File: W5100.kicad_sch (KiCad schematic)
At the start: 8 parts, among them U2 W5100

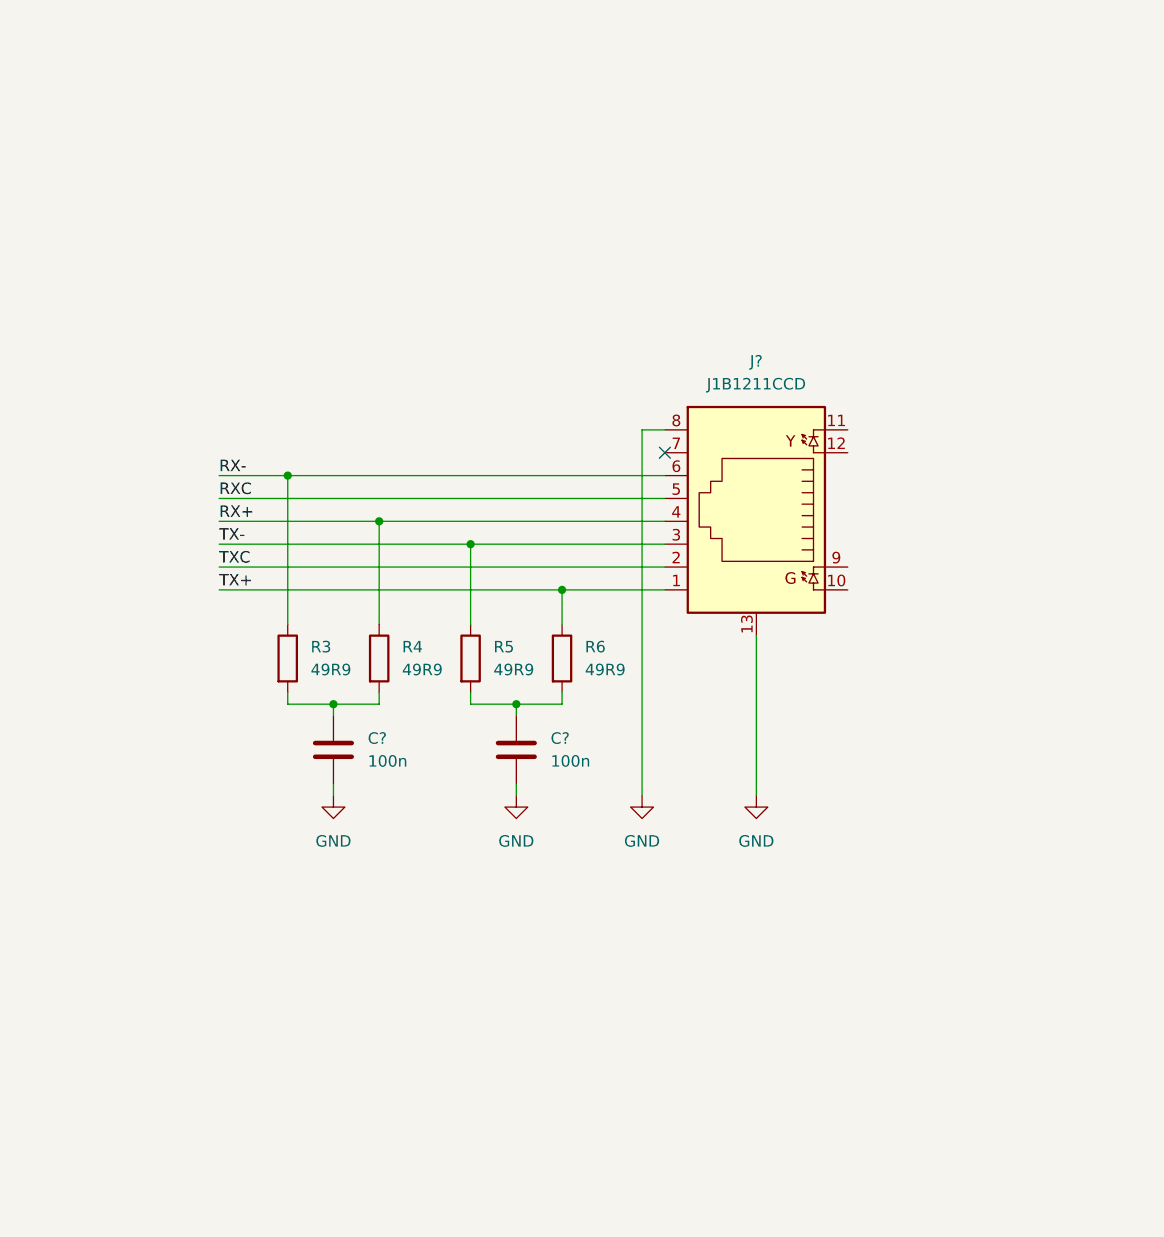
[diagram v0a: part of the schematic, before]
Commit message: Added RJ45
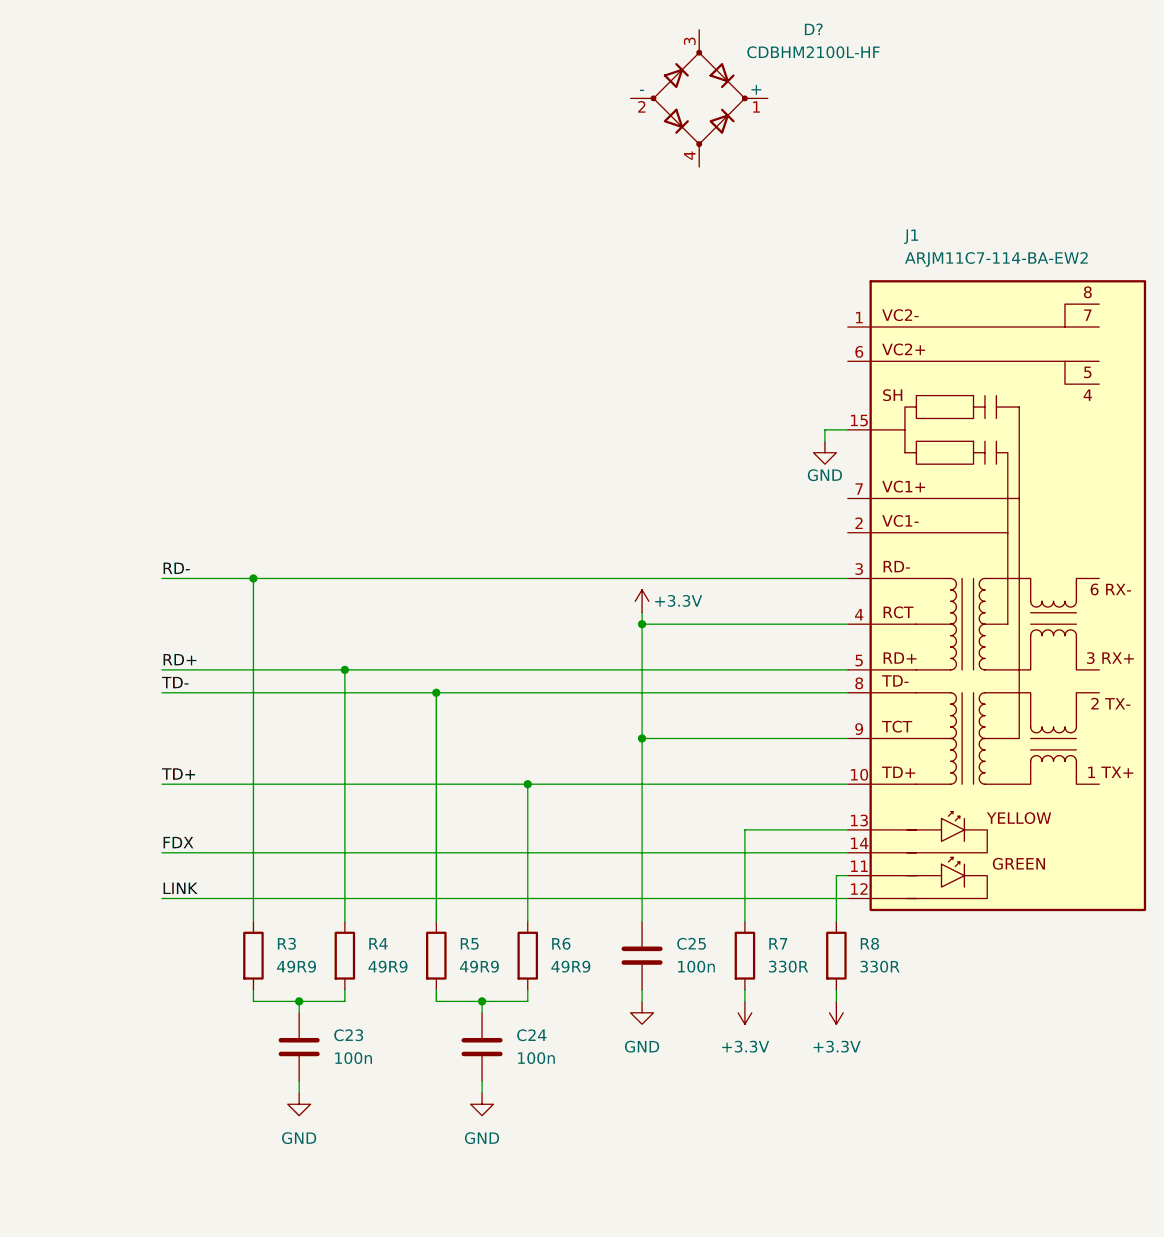
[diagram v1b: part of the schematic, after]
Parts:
- removed J?: J1B1211CCD, Connector_RJ:RJ45_Cetus_J1B1211CCD_Horizontal, symbol wiznet:J1B1211CCD
- added C25: 100n, symbol Device:C
- added D?: CDBHM2100L-HF, comchip:CDBHM2100L-HF, symbol Device:D_Bridge_+-AA
- added J1: ARJM11C7-114-BA-EW2, symbol abracon:ARJM11C7-114-BA-EW2
- added R7, R8: 330R, symbol Device:R
- gave numbers to parts that had none: 2
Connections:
- net GND: now also C25.2, J1.15
- net RX+ renamed RD+
- net RD+: now also J1.5
- net RX- renamed RD-
- net RD-: now also J1.3
- net TX+ renamed TD+
- net TD+: now also J1.10
- net TX- renamed TD-
- net TD-: now also J1.8
- new net: J1.11, R8.1
- new net: J1.13, R7.1
- new net +3.3V: C25.1, J1.4, J1.9, R7.2, R8.2
- new net FDX: J1.14
- new net LINK: J1.12
- no-connect marks 1 -> 0
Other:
- moved on the sheet: C23, C24, R3, R4, R5, R6

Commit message: Finishe PoE and ethernet
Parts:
- removed D?: CDBHM2100L-HF, comchip:CDBHM2100L-HF, symbol Device:D_Bridge_+-AA
- added C26: 1000u, symbol Device:C_Polarized
- added C27: 100u, symbol Device:C
- added C28, C29: 1n 3kV, symbol Device:C
- added C30, C36: 10n, symbol Device:C
- added C31, C33: 10p, symbol Device:C
- added C32: 10u, symbol Device:C_Polarized
- added C34, C35, C37: 1u, symbol Device:C
- added C38, C39, C40, C41, C42, C43, C44, C45, C47, C58, C59, C62: 100n, symbol Device:C
- added C46: 3u3, symbol Device:C
- added C48, C49, C54, C55: 10u, symbol Device:C
- added C50, C51, C52, C53, C56, C57, C60, C61: 1n, symbol Device:C
- added D1: PDS1040, symbol Device:D_Schottky
- added D2: 1N4148W, Diode_SMD:D_SOD-123, symbol Diode:1N4148W
- added D3: DFLT30A, symbol Device:D_Zener
- added FB1, FB2, FB3: 1u, symbol Device:FerriteBead_Small
- added L4: 1u, symbol Device:L
- added R10, R9: 10k, symbol Device:R
- added R11: 300R 1%, symbol Device:R
- added R12: 12k 1%, symbol Device:R
- added R13: 36k5, symbol Device:R
- added R14: 12k1, symbol Device:R
- added R15: 1M, symbol Device:R
- added R16: 2k2, symbol Device:R
- added R17: 5k1, symbol Device:R
- added R18: 24k3, symbol Device:R
- added R19: 48R7, symbol Device:R
- added T1: FA2805, symbol coilcraft:FA2805
- added U3: TLV431DBZ, Package_TO_SOT_SMD:SOT-23, symbol Reference_Voltage:TL431DBZ
- added U4: VO615A, symbol Isolator:VO615A
- added U5: SI3402, symbol skyworks:SI3402
- added Y2: 25MHz, Crystal:Crystal_SMD_3225-4Pin_3.2x2.5mm, symbol Device:Crystal_GND24
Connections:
- net +3.3V is gone; now on net +3V3A: C25.1, J1.4, J1.9, R7.2, R8.2
- net FDX: now also U2.70 (FDXLED)
- net GND: now also U2.13 (GNDD), U2.14 (GNDD), U2.17 (GNDD), U2.32 (GNDD), U2.34 (TEST_MODE3), U2.35 (TEST_MODE2), U2.36 (TEST_MODE1), U2.37 (TEST_MODE0), U2.43 (GNDD), U2.63 (OPMODE0), U2.64 (OPMODE1), U2.65 (OPMODE2), U2.68 (GNDD), C26.2, C27.2, C29.1, C31.2, C33.2, C39.2, C41.2, C42.2, C43.2, C44.2, C45.2, C46.2, C47.2, C48.2, C49.2, FB3.1, R12.2, R14.2, T1.10, T1.9, U3.3 (A), Y2.2, Y2.4; no longer C23.2, C24.2, C25.2, J1.15
- net LINK: now also U2.66 (LINKLED)
- net RD+: now also U2.5 (RXIP)
- net RD-: now also U2.6 (RXIN)
- net TD+: now also U2.8 (TXOP)
- net TD-: now also U2.9 (TXON)
- net at J1.1: now also C60.2, C61.1, U5.14 (CT1)
- net at J1.2: now also C50.2, C51.1, U5.10 (SP2)
- net at J1.6: now also C56.2, C57.1, U5.13 (CT2)
- net at J1.7: now also C52.2, C53.1, U5.11 (SP1)
- net at U2.1 (RSET_BG): now also R11.1
- net GNDA: now reaches U2.10 (GNDA), U2.4 (GNDA), U2.77 (GNDA)
- net GNDA: now also C23.2, C24.2, C25.2, C54.2, C55.2, C58.2, C59.2, C62.2, FB3.2
- net +1V8: now reaches U2.11 (1V8_OUT)
- net +1V8: now also U2.15 (VCC1V8D), U2.16 (VCC1V8D), U2.33 (VCC1V8D), U2.69 (VCC1V8D), C39.1, C41.1, C43.1, C44.1, C46.1, C48.1, FB1.1
- net +3V3: now reaches U2.12 (VCC3V3D), U2.18 (VCC3V3D), U2.44 (VCC3V3D)
- net +3V3: now also C42.1, C45.1, C47.1, C49.1, FB2.1, R10.1, R9.1
- net +3V3A: now reaches U2.2 (VCC3V3A)
- net +3V3A: now also C55.1, C59.1, FB2.2
- net MISO: now reaches U2.27 (MISO)
- net MOSI: now reaches U2.28 (MOSI)
- net ~{CS}: now reaches U2.29 (~{SCS})
- net CLK: now reaches U2.30 (SCLK)
- net at U2.31 (SEN): now also R10.2
- net ~{INT}: now reaches U2.56 (~{INT})
- net ~{RST}: now reaches U2.59 (~{RESET})
- net ~{RST}: now also R9.2
- net +1V8A: now reaches U2.7 (VCC1V8A), U2.74 (VCC1V8A)
- net +1V8A: now also C54.1, C58.1, C62.1, FB1.2
- net at U2.75 (XTLN): now also C31.1, R15.2, Y2.1
- net at U2.76 (XTLP): now also C33.1, R15.1, Y2.3
- new net: C30.1, R13.2, R14.1, U3.2 (REF)
- new net: C30.2, R16.2, U3.1 (K)
- new net: C28.2, C32.1, C34.1, C35.1, C37.1, C40.1, C50.1, C52.1, C56.1, C60.1, D2.1 (K), R18.1, T1.1, U5.12 (VPOSF), U5.20 (FB)
- new net: C29.2, D3.1 (K), T1.2, U5.18 (SWO)
- new net: D1.2 (A), T1.7, T1.8
- new net: C38.1, R17.2, U5.3 (VDD)
- new net: C32.2, C34.2, C35.2, C36.2, C37.2, C38.2, C40.2, U4.3, U5.15 (VSSA), U5.19 (VSS2), U5.7 (HSO)
- new net: C36.1, R17.1, U4.4, U5.1 (EROUT)
- new net: R18.2, U5.6 (RDET)
- new net: R19.1, U5.8 (RCL)
- new net: C51.2, C53.2, C57.2, C61.2, R19.2, U5.9 (VNEG)
- new net: D2.2 (A), D3.2 (A)
- new net: C27.1, D1.1 (K), L4.2
- new net: R11.2, R12.1
- new net: R16.1, U4.2
- new net 5V: C26.1, C28.1, L4.1, R13.1, U4.1
- new net Earth: J1.15
- no-connect marks 0 -> 30
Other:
- note added: "OPMODE 000 = Auto-negotiation enabled with all capabilities"
- moved on the sheet: C23, C24, C25, J1, R3, R4, R5, R6, R7, R8, U2
